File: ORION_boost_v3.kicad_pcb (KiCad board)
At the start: 4 copper layers, 92 x 124 mm, 141 parts, among them J1 Conn_02x04_Odd_Even, J2 Conn_01x10, J3 Conn_01x03, J4 Conn_01x03, J5 Conn_01x01, J6 Conn_01x01, J7 Conn_01x02, J8 Conn_01x02, J9 Conn_01x02, P1 CONN_01X06, P2 CONN_01X02, P3 CONN_01X02, P4 CONN_01X02, P5 CONN_01X02, P6 CONN_01X02, P7 CONN_01X02, Q1 Q_NMOS_GDS, Q2 Q_NMOS_GDS, Q3 Q_NMOS_GSD, Q4 Q_PMOS_GDS, Q5 Q_NMOS_GDS, Q6 Q_NMOS_GDS, Q7 Q_NMOS_GDS, Q8 Q_NMOS_GDS, Q9 Q_NMOS_GDS, SW1 SW_Push, SW2 SW_Push, SW3 SW_Push, U1 STM32F303CBTx, U2 LTC2875-S8, U4 INA199, X1 ceralock

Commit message: 天丼マン
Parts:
- added Q10: Q_NMOS_GSD, Package_TO_SOT_SMD:SOT-23, B.Cu at (132.0, 141.5)
- added R41: 100, Resistor_SMD:R_0603_1608Metric, B.Cu at (132.0, 136.5)
- added R42: 1k, Resistor_SMD:R_0603_1608Metric, B.Cu at (132.0, 139.0)
- D6: footprint Diode_SMD:D_0603_1608Metric -> Diode_SMD:D_PowerDI-123
- P4: moved to F.Cu
- moved D6 47.5 mm to (132.0, 146.0), turned to -90 degrees
- moved R17 6.02 mm to (128.5, 113.0), turned to 0 degrees
- moved C11 4.74 mm to (130.0, 115.0), turned to 0 degrees
- moved U4 3.81 mm to (129.5, 118.0), turned to -90 degrees
- moved C29 3.54 mm to (112.0, 90.0)
- moved R38 3.50 mm to (110.0, 90.0)
- moved C4 3.04 mm to (121.0, 103.5), turned to 90 degrees
- moved R28 2.92 mm to (133.0, 111.0)
- moved R32 2.92 mm to (133.0, 119.0), turned to -90 degrees
- moved C9 2.50 mm to (110.5, 112.0), turned to 180 degrees
- moved R10 2.12 mm to (110.5, 110.0), turned to 0 degrees
- moved Q3 1.58 mm to (133.0, 115.5)
- moved R31 1.58 mm to (133.0, 112.5), turned to 180 degrees
- moved J9 1.12 mm to (105.0, 110.5), turned to 0 degrees
- moved C19 1.00 mm to (138.0, 96.0)
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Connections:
- C10 pad 2: Net-(C10-Pad2) -> /TEMP_FET
- D6 pad 1: /LOGIC_POWER -> Net-(D6-Pad1)
- D6 pad 2: Net-(D6-Pad2) -> Net-(D10-Pad1)
- P1 pad 2: Net-(D6-Pad2) -> unconnected-(P1-Pad2)
- R11 pad 1: Net-(C10-Pad2) -> /TEMP_FET
- SW2 pad 1: /SW1 -> /SW_1
- SW3 pad 1: /SW2 -> /SW_2
- TH1 pad 2: Net-(C10-Pad2) -> /TEMP_FET
- U1 pad 28: /TEMP_COIL_3 -> unconnected-(U1-Pad28)
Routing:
- net +3.3V: track 75.2 -> 200.8 mm, vias 2 -> 8
- net +12V: track 44.5 -> 128.2 mm, vias 2 -> 6
- net GND: track 87.4 -> 143.6 mm, vias 6 -> 11
- net /NRST: track 1.77 -> 54.3 mm, vias 1 -> 2
- net /SW_1: track 0.00 -> 52.1 mm, vias 0 -> 2
- net /TEMP_COIL_2: track 0.00 -> 51.2 mm, vias 0 -> 2
- net /BOOST_V: track 6.43 -> 56.1 mm, vias 1 -> 4
- net /SW_2: track 0.00 -> 48.7 mm, vias 0 -> 2
- net /LED_CURRENT: track 0.00 -> 46.7 mm, vias 0 -> 3
- net /BATT_V: track 0.00 -> 45.5 mm, vias 0 -> 2
- net /KICK_2: track 1.07 -> 35.3 mm, vias 1 -> 2
- net /LED_3: track 0.71 -> 34.7 mm, vias 1 -> 2
- net Net-(D17-Pad1): track 5.68 -> 39.6 mm, vias 0 -> 3
- net /LED_2: track 0.71 -> 34.1 mm, vias 1 -> 2
- net /LED_1: track 0.71 -> 33.5 mm, vias 1 -> 2
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- added copper zone on In1.Cu, net +BATT
- added copper zone on In2.Cu, net +BATT
- added copper zone on In1.Cu, net /CAP_450V
- added copper zone on In2.Cu, net /CAP_450V
- added copper zone on In1.Cu, net GND
- added copper zone on In2.Cu, net GND
- added copper zone on B.Cu, net Net-(D17-Pad1)
- added copper zone on In1.Cu, net Net-(D19-Pad2)
- added copper zone on In2.Cu, net Net-(D19-Pad2)
- added copper zone on In1.Cu, net Net-(D20-Pad2)
- added copper zone on In2.Cu, net Net-(D20-Pad2)
- added copper zone on In1.Cu, net Net-(D21-Pad2)
- added copper zone on In2.Cu, net Net-(D21-Pad2)
- added copper zone on B.Cu, net Net-(F1-Pad1)
- added copper zone on F.Cu, net Net-(F1-Pad1)
- added copper zone on In1.Cu, net Net-(F1-Pad1)
- added copper zone on In2.Cu, net Net-(F1-Pad1)
- added copper zone on B.Cu, net Net-(F1-Pad2)
- added copper zone on F.Cu, net Net-(F1-Pad2)
- added copper zone on In1.Cu, net Net-(F1-Pad2)
- added copper zone on In2.Cu, net Net-(F1-Pad2)
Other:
- board text removed: "1"
- board text removed: "2"
- board text removed: "21"
- board text removed: "3V"

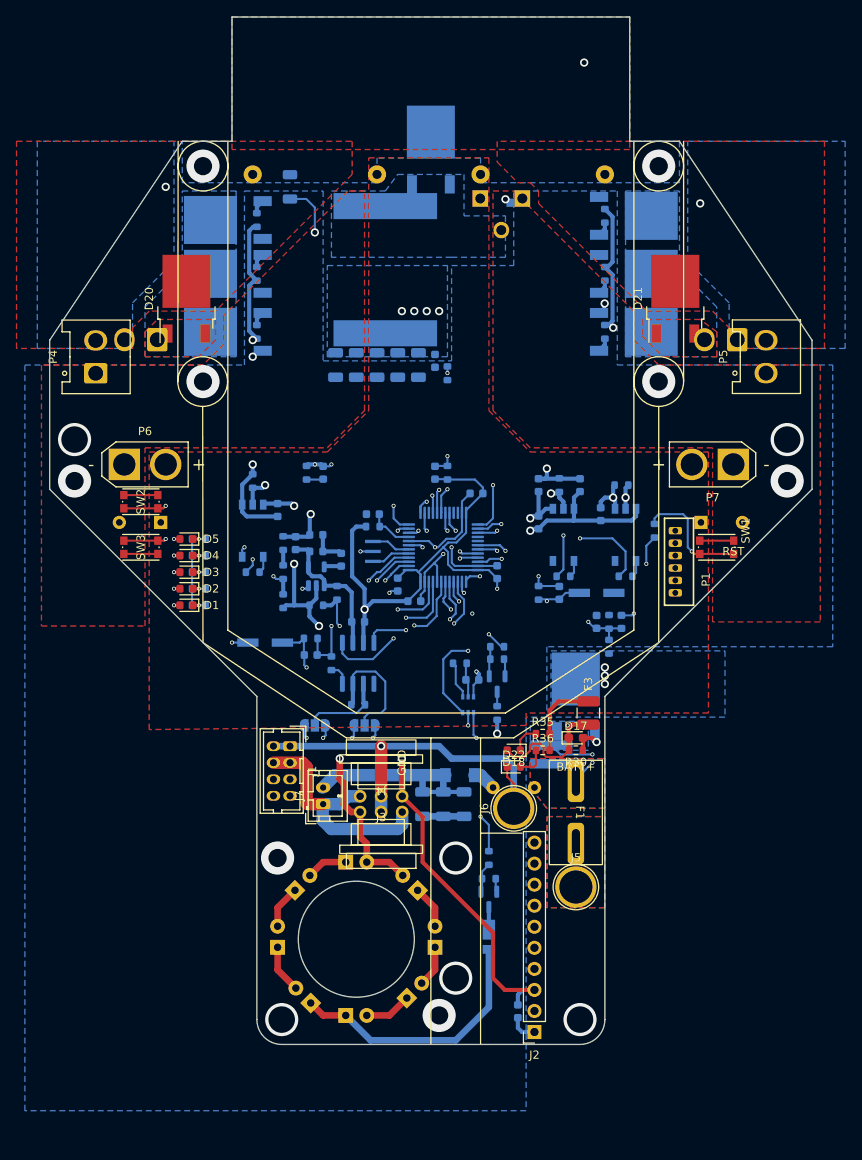
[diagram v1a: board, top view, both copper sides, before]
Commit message: ビアうち、レイアウト調整、GNDライン構築、メカ寸法調整(途中)
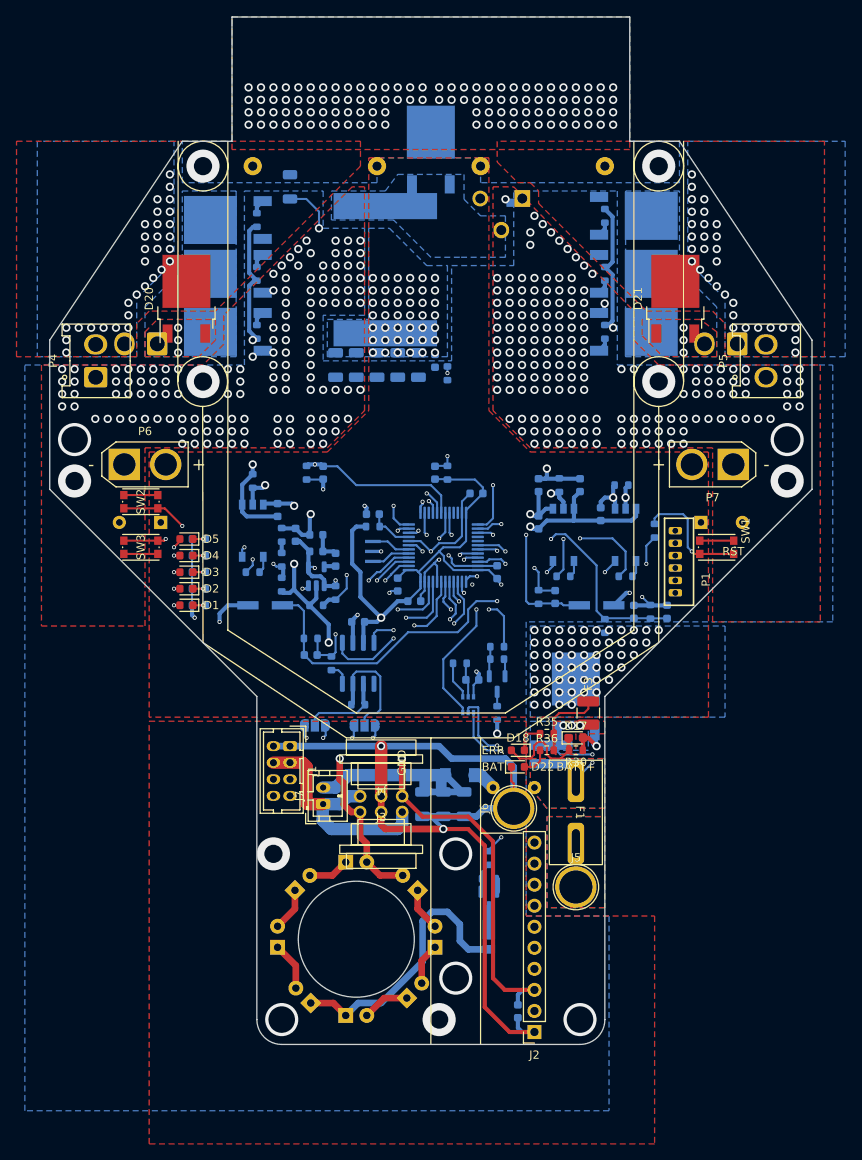
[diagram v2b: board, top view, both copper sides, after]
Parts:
- moved D15 5.63 mm to (153.5, 106.8)
- moved R15 5.14 mm to (151.5, 106.8)
- moved C12 4.66 mm to (149.5, 106.8)
- moved J9 4.50 mm to (105.0, 106.0)
- moved R14 2.55 mm to (146.0, 108.5)
- moved R18 2.01 mm to (107.0, 103.5)
- moved R19 1.51 mm to (107.0, 100.5)
- moved J8 1.50 mm to (145.0, 106.0)
- moved R20 1.02 mm to (107.0, 97.5)
- moved C27 1.00 mm to (146.0, 53.0)
- moved C28 1.00 mm to (103.5, 53.0)
- moved C31 1.00 mm to (108.7, 97.5)
- moved C7 0.71 mm to (140.0, 105.0)
- moved C30 0.67 mm to (113.5, 100.5)
- moved D18 0.50 mm to (135.5, 123.5)
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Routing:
- net GND: track 143.6 -> 346.4 mm, vias 11 -> 323
- net +BATT: track 9.95 -> 32.9 mm, vias 7 -> 97
- net Net-(C15-Pad2): track 24.6 -> 32.3 mm
- net Net-(C21-Pad2): track 41.7 -> 48.4 mm
- net /GD_16P: track 23.4 -> 17.0 mm
- net /BATT_V: track 45.5 -> 39.6 mm
- net /TEMP_COIL_2: track 51.2 -> 46.4 mm
- net +3.3V: track 200.8 -> 204.7 mm
- net Net-(PC3-Pad5): track 42.4 -> 45.4 mm
- net /SWCLK: track 30.5 -> 27.8 mm
- net /GD_16M: track 30.3 -> 28.0 mm
- net Net-(D17-Pad1): track 39.6 -> 37.6 mm, vias 3 -> 5
- net +12V: track 128.2 -> 130.1 mm
- net /LED_CURRENT: track 46.7 -> 48.2 mm
- net /LED_3: track 34.7 -> 36.2 mm
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- added copper zone on F.Cu, net Net-(D17-Pad1)
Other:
- board text added: "BAT"
- board text added: "ERR"

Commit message: シルク･ビア最終調整、銅線貼り付け猶予
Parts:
- moved C29 2.00 mm to (112.0, 92.0)
- moved R38 2.00 mm to (110.0, 92.0)
- moved C10 1.80 mm to (126.5, 91.5)
- moved R11 1.80 mm to (128.0, 91.5)
- moved R14 1.50 mm to (147.5, 108.5)
- moved R21 0.71 mm to (103.0, 91.5), turned to 0 degrees
- moved R22 0.71 mm to (147.5, 92.0)
- moved C6 0.50 mm to (133.0, 102.5)
- moved R17 0.50 mm to (129.0, 113.0)
- turned JP1 to 0 degrees
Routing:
- net GND: track 346.4 -> 371.4 mm, vias 323 -> 353
- net /SWDIO: track 24.6 -> 26.5 mm
- net /KICK_2: track 34.1 -> 32.3 mm
- net /KICK_1: track 31.6 -> 33.4 mm
- net /KICK_2_SOURCE: track 24.7 -> 26.4 mm
- net /CAN1_H: track 17.7 -> 19.4 mm
- net +3.3V: track 204.7 -> 203.4 mm
- net Net-(C21-Pad2): track 48.4 -> 49.6 mm
- net /TEMP_FET: track 27.2 -> 28.4 mm
- net /BOOST_SW: track 26.4 -> 27.5 mm
- net /TEMP_COIL_2: track 46.4 -> 45.4 mm
- net /CAN0_H: track 16.5 -> 15.6 mm
- net /KICK_2_GATE: track 37.8 -> 37.1 mm
- net /TEMP_COIL_1: track 21.3 -> 20.6 mm
- net /CAN1_L: track 10.3 -> 10.9 mm
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- added copper zone on F.Cu, net Net-(D19-Pad2)
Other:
- board size 92 x 124 mm -> 92 x 119 mm
- board text added: "0 1 0 1"
- board text added: "1"
- board text added: "12V"
- board text added: "2"
- board text added: "3"
- board text added: "3.3V"
- board text added: "CAP"
- board text added: "COIL_1"
- board text added: "COIL_2"
- board text added: "KICK1"
- board text added: "KICK2"
- board text added: "SRT"
- board text added: "STLINK"
- board text removed: "ERR"

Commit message: ベタパターンの調整
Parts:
- moved JP2 5.50 mm to (116.5, 120.5)
- moved JP1 5.00 mm to (112.0, 120.5)
- moved R37 2.04 mm to (110.0, 55.9)
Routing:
- net /CAN_H: track 14.7 -> 7.63 mm
- net /CAN1_H: track 19.4 -> 12.4 mm
- net /CAN0_H: track 15.6 -> 9.59 mm
- net /CAN0_L: track 7.45 -> 12.4 mm
- net +BATT: track 32.9 -> 37.8 mm
- net /CAN_L: track 10.3 -> 5.33 mm
- net /CAN1_L: track 10.9 -> 15.4 mm
- net /BATT_CS: track 31.0 -> 35.0 mm
- net /BOOST_V: track 56.6 -> 54.3 mm
- net +3.3V: track 203.4 -> 202.5 mm
- net /GD_16M_PWM: track 29.5 -> 28.7 mm
- net /TEMP_COIL_1: track 20.6 -> 19.9 mm
- net Net-(D21-Pad2): vias 3 -> 8
- net Net-(D20-Pad2): vias 3 -> 8
- net Net-(D19-Pad2): vias 5 -> 6
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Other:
- board text added: "2022/12/10 designed by ibis"
